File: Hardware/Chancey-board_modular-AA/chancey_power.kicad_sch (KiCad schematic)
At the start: 7 parts

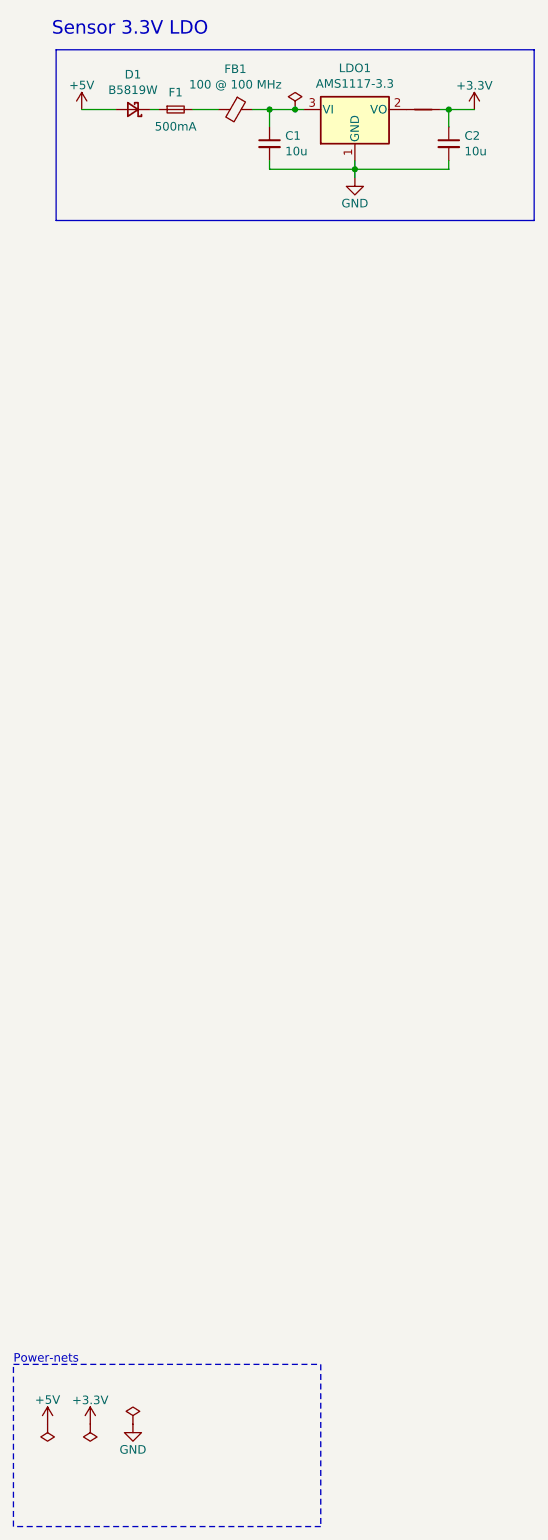
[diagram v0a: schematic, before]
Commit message: Changed many global labels to hierarchical and local labels.
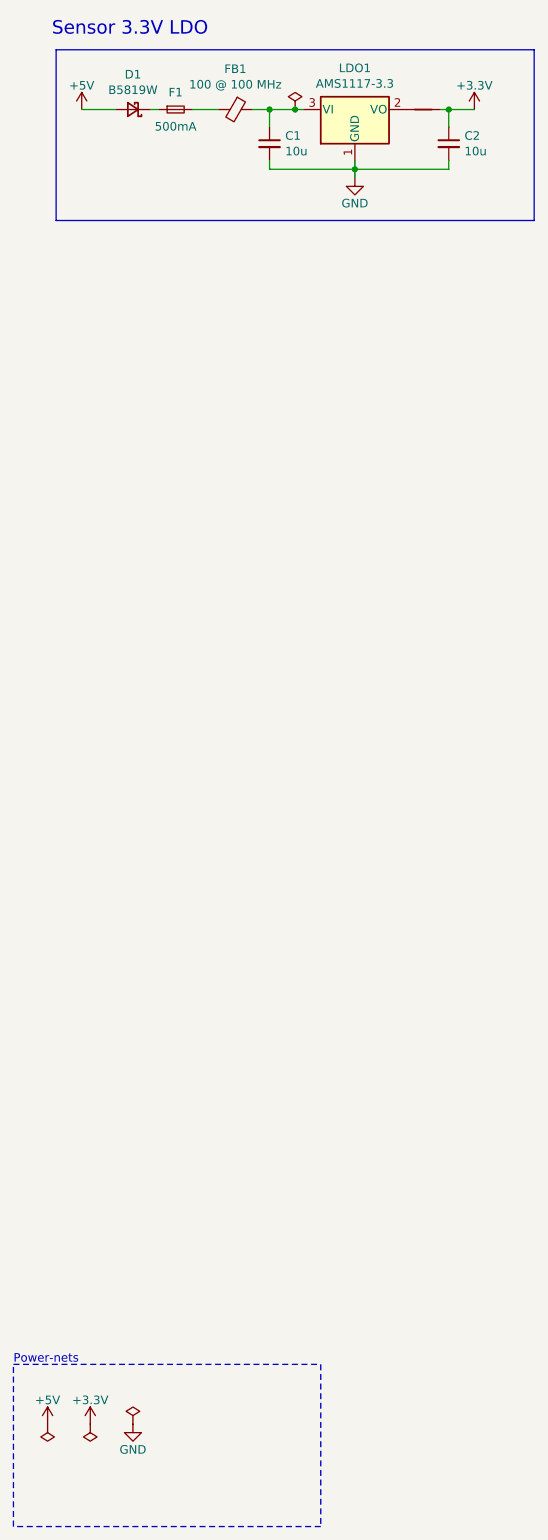
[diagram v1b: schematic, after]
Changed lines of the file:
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@@
       (effects (font (size 1.27 1.27)) hide)
     )
-    (property "Value" "+5V" (at 31.75 34.4955 0)
+    (property "Value" "+5V" (at 31.75 34.544 0)
       (effects (font (size 1.27 1.27)))
     )
@@
       (effects (font (size 1.27 1.27)) hide)
     )
-    (property "Value" "+5V" (at 26.67 230.0755 0)
+    (property "Value" "+5V" (at 26.67 230.124 0)
       (effects (font (size 1.27 1.27)))
     )
